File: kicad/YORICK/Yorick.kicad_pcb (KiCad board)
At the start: 2 copper layers, 124 x 112 mm, 68 parts, among them J1 Conn_01x12, J2 AVR-ISP-6, J3 AudioJack2_SwitchT, J4 USB_B_Micro, J5 AudioJack2_SwitchT, Q1 Q_NJFET_DSG, Q2 Q_NJFET_DSG, SW1 SW_Push, SW2 SW_Push, U1 4069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

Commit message: Finalising gerbers before sending off rev1.1
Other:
- board text added: "YORICK PLATFORM v1.1"
- board text removed: "YORICK PLATFORM v1.0"
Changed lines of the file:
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@@
     (effects (font (size 1 1) (thickness 0.15)) (justify left bottom))
   )
-  (gr_text "YORICK PLATFORM v1.0" (at 117.2144 38.231708) (layer "F.SilkS")
+  (gr_text "YORICK PLATFORM v1.1" (at 117.2144 38.231708) (layer "F.SilkS")
     (effects (font (size 1.5 1.5) (thickness 0.15)) (justify left bottom))
   )

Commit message: Updating bill of materials
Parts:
- Q1, Q2: value Q_NJFET_DSG -> J113
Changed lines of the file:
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@@
   (title_block
     (date "2023-07-19")
-    (rev "rev02")
+    (rev "rev1.1")
     (comment 2 "creativecommons.org/licenses/by/4.0")
     (comment 3 "License: CC BY 4.0")
@@
         (effects (font (size 1 1) (thickness 0.15)))
     )
-    (fp_text value "Q_NJFET_DSG" (at 2.54 2.79) (layer "F.Fab") hide
+    (fp_text value "J113" (at 2.54 2.79) (layer "F.Fab") hide
         (effects (font (size 1 1) (thickness 0.15)))
     )
@@
         (effects (font (size 1 1) (thickness 0.15)))
     )
-    (fp_text value "Q_NJFET_DSG" (at 2.54 2.79) (layer "F.Fab") hide
-        (effects (font (size 1 1) (thickness 0.15)))
-    )
+    (fp_text value "J113" (at 2.54 2.79) (layer "F.Fab") hide
+        (effects (font (size 1 1) (thickness 0.15)))
+    )

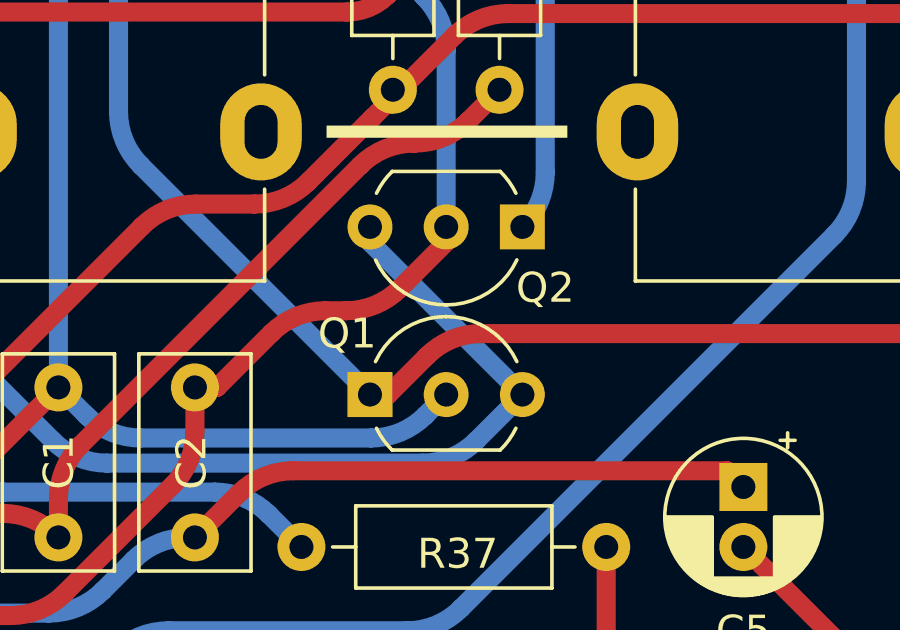
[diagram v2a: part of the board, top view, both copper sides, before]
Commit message: Refreshing project for kicad 8
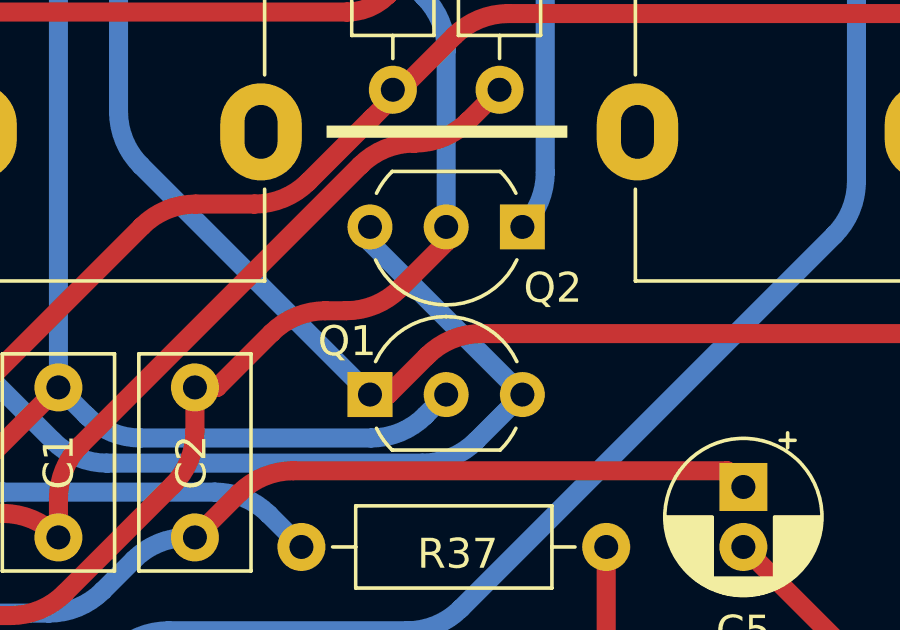
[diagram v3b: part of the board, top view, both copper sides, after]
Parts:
- Q1, Q2: footprint Rumblesan_Standard_Parts:TO-92_Inline_Wide -> Package_TO_SOT_THT:TO-92_Inline_Wide
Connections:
- C11 pad 2: Net-(J5-T) -> Net-(U2A-+)
- C5 pad 2: Net-(J3-T) -> Net-(C5-Pad2)
- R22 pad 2: Net-(J5-T) -> Net-(U2A-+)
- U2 pad 3: Net-(J5-T) -> Net-(U2A-+)
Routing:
- net Net-(U2A-+): track 0.00 -> 25.5 mm
- net Net-(J5-T): track 25.5 -> 0.00 mm
- net Net-(J3-T): track 14.5 -> 0.00 mm
- net Net-(C5-Pad2): track 0.00 -> 14.5 mm

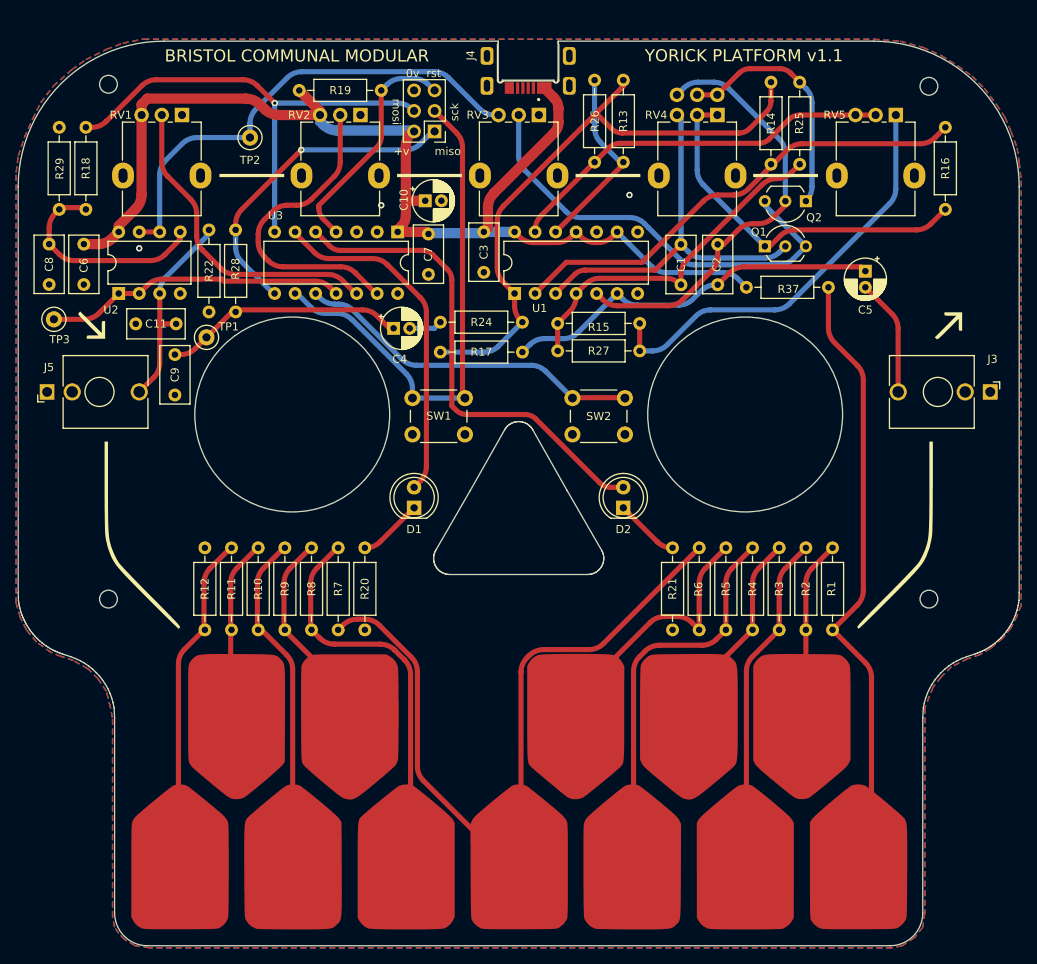
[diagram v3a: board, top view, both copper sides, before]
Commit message: Updating with USB C socket
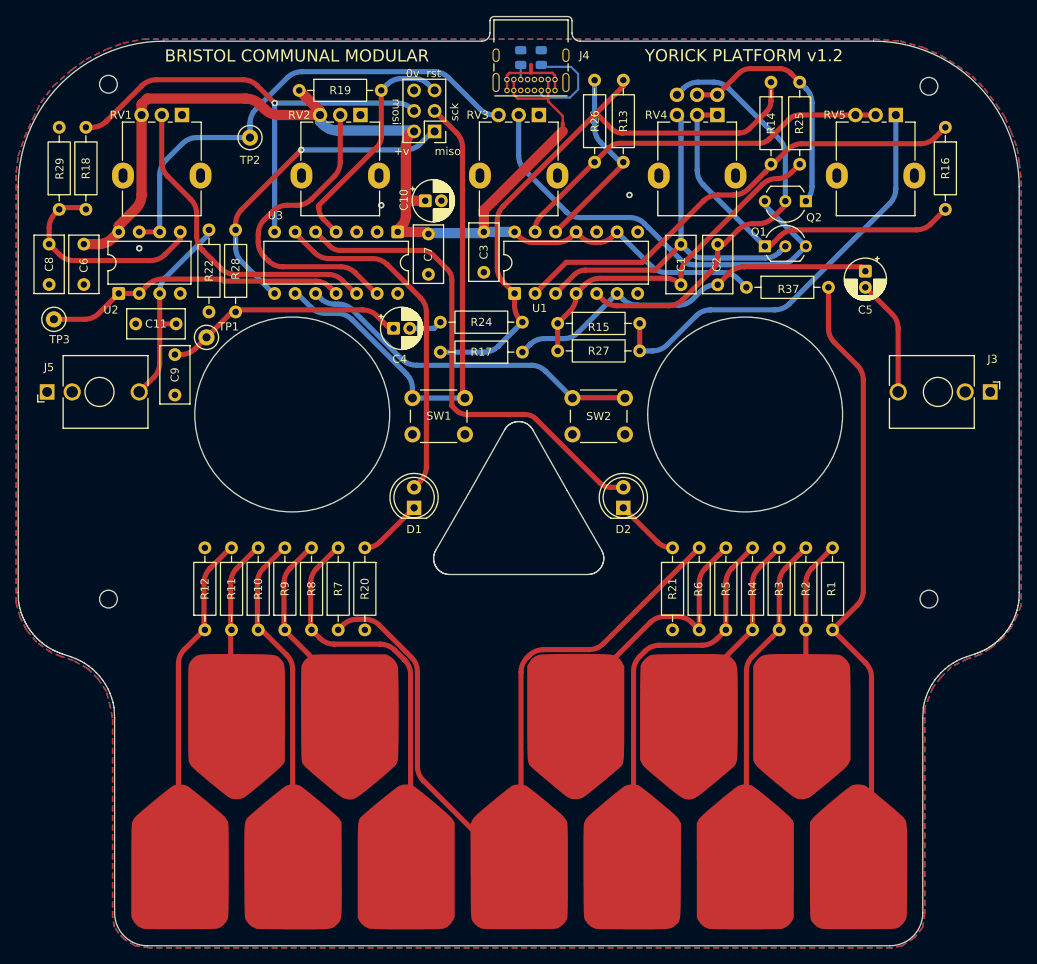
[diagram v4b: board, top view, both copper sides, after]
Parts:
- removed REF**: facelines, Yorick:Facelines
- added NT1: NetTie_2, NetTie:NetTie-2_SMD_Pad0.5mm, F.Cu at (107.1, 46.2)
- added NT2: NetTie_2, NetTie:NetTie-2_SMD_Pad0.5mm, F.Cu at (103.1, 39.0)
- added R23: 5k1, Resistor_SMD:R_0805_2012Metric, B.Cu at (104.4, 37.6)
- added R30: 5k1, Resistor_SMD:R_0805_2012Metric, B.Cu at (101.9, 37.6)
- J4: value USB_B_Micro -> USB_C_Receptacle_USB2.0_16P; footprint Yorick:AMPHENOL_10103593-0001LF-Power -> Connector_USB:USB_C_Receptacle_GCT_USB4085
- moved J4 5.42 mm to (106.1, 41.7)
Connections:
- net /MCU_DIN2 renamed MCU_SCK
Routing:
- net /usbc-cc1: track 0.00 -> 12.6 mm
- net /usbc-power: track 0.00 -> 12.5 mm
- net /usbc-gnd: track 0.00 -> 9.92 mm
- net VCC: track 147.2 -> 141.6 mm
- net /usbc-cc2: track 0.00 -> 1.81 mm
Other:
- board size 124 x 112 mm -> 124 x 115.1 mm
- board text added: "YORICK PLATFORM v${REVISION}"
- board text removed: "YORICK PLATFORM v1.1"
